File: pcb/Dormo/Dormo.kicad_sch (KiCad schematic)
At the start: 41 parts, among them J1 Conn_01x02_Socket, J2 USB_C_Receptacle_USB2.0_16P, Q1 AO3401A, SW1 SW_DPST, U1 ESP32-C3, U2 MIC5504-3.3YM5, U3 BRCL4054BME, Y1 40MHz

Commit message: cleanup schematic
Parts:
- removed C1: C_Small, symbol Device:C_Small
- removed C3: 100nF, Capacitor_SMD:C_0603_1608Metric_Pad1.08x0.95mm_HandSolder, symbol Device:C_Small
- removed C5: 10uF, Capacitor_SMD:C_0805_2012Metric_Pad1.18x1.45mm_HandSolder, symbol Device:C_Small
- removed J1: Conn_01x02_Socket, symbol Connector:Conn_01x02_Socket
- removed R1: R_Small, symbol Device:R_Small
- added J3: FPC, 6P, P=0.5mm, Connector_FFC-FPC:Hirose_FH12-6S-0.5SH_1x06-1MP_P0.50mm_Horizontal, symbol Connector_Generic:Conn_01x06
- added J4: Conn_01x02, symbol Connector_Generic:Conn_01x02
- SW1: value SW_DPST -> ~
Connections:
- net +3V3: now also J3.6 (Pin_6)
- net +VBAT: now also J3.4 (Pin_4), J4.1 (Pin_1)
- net BTN: now also J3.1 (Pin_1)
- net GND: now also J3.5 (Pin_5), J4.2 (Pin_2)
- net GPIO02: now also J3.2 (Pin_2)
- net GPIO08: now also J3.3 (Pin_3)
- net at C4.1, Y1.3: now also U1.30 (XTAL_P); no longer U1.29 (XTAL_N)
- net at C10.1, Y1.1: now also U1.29 (XTAL_N); no longer U1.30 (XTAL_P)
- net GPIO06: now reaches U1.12 (MTCK)
- net GPIO07: now reaches U1.13 (MTDO)
- net GPIO09: now reaches U1.15 (GPIO9)
- net GPIO10: now reaches U1.16 (GPIO10)
- net GPIO12: now reaches U1.19 (SPIHD)
- net GPIO13: now reaches U1.20 (SPIWP)
- net GPIO14: now reaches U1.21 (SPICS0)
- net GPIO15: now reaches U1.22 (SPICLK)
- net GPIO16: now reaches U1.23 (SPID)
- net GPIO17: now reaches U1.24 (SPIQ)
- net GPIO20: now reaches U1.27 (U0RXD)
- net GPIO21: now reaches U1.28 (U0TXD)
- net GPIO03 renamed EN_VSENSE
- net USB+ renamed GPIO19
- net USB- renamed GPIO18
- net VDD_SPI renamed GPIO11
- no-connect marks 3 -> 2
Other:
- note added: "Battery connector"
- note added: "Check footprint"
- note added: "Pin mapping"
- note added: "Power latch"
- note added: "USB-C connector"
- note added: "VBAT sensing"
- note added: "expander connector"
- note added: "pullups"
- moved on the sheet: AE1, C10, C11, C12, C13, C14, C2, C4, C6, C7, C8, C9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

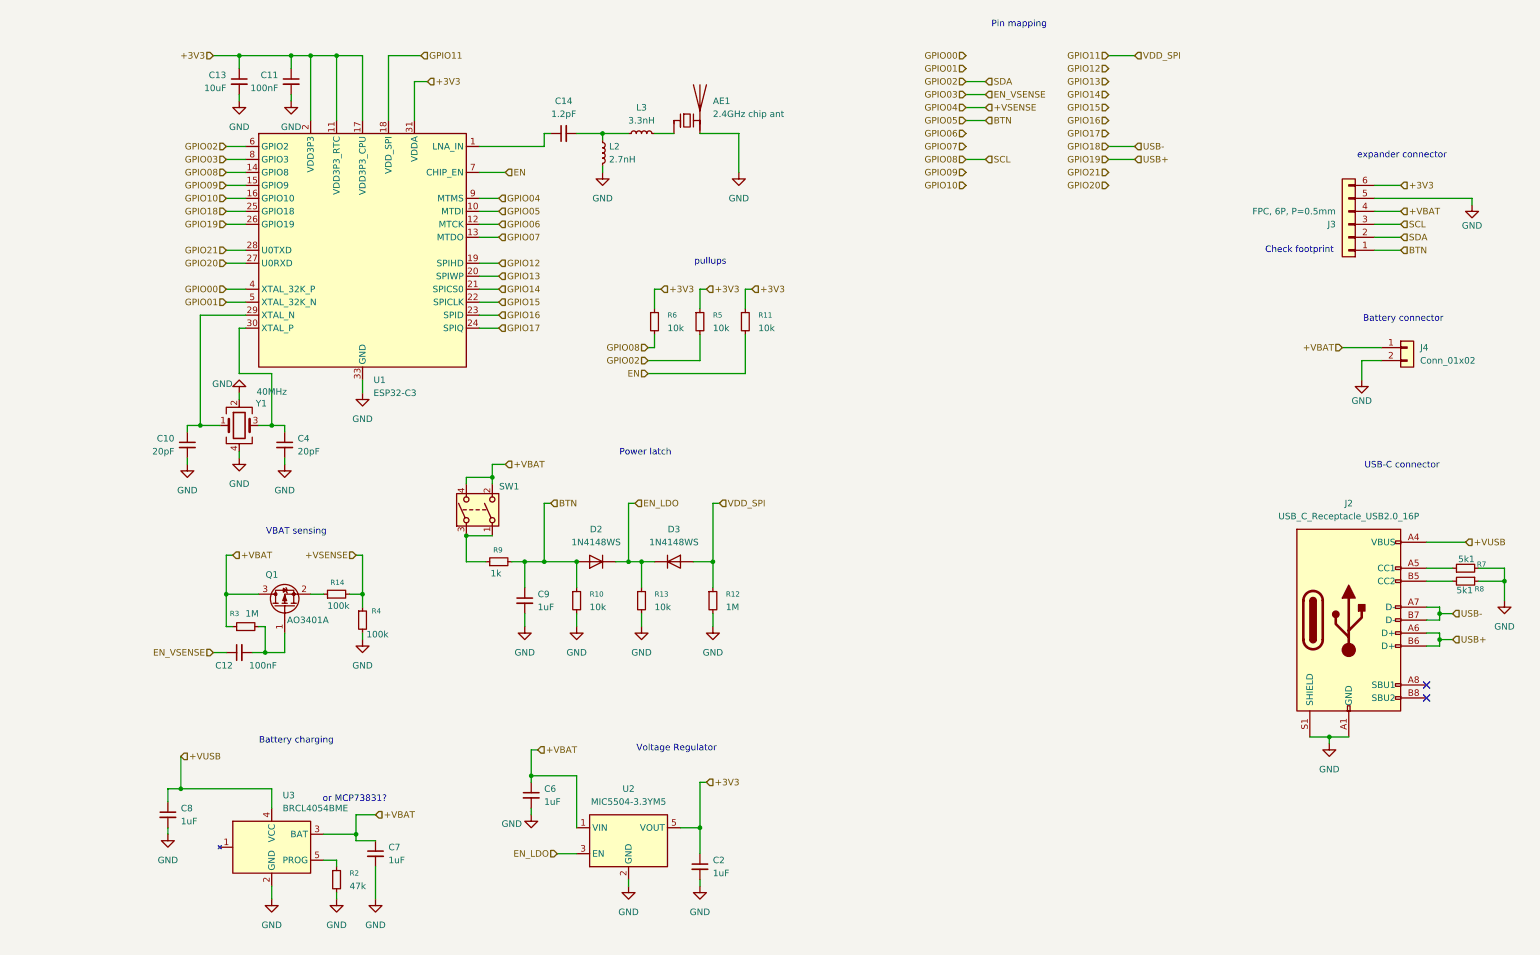
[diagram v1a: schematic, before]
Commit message: added button matrix in schematic
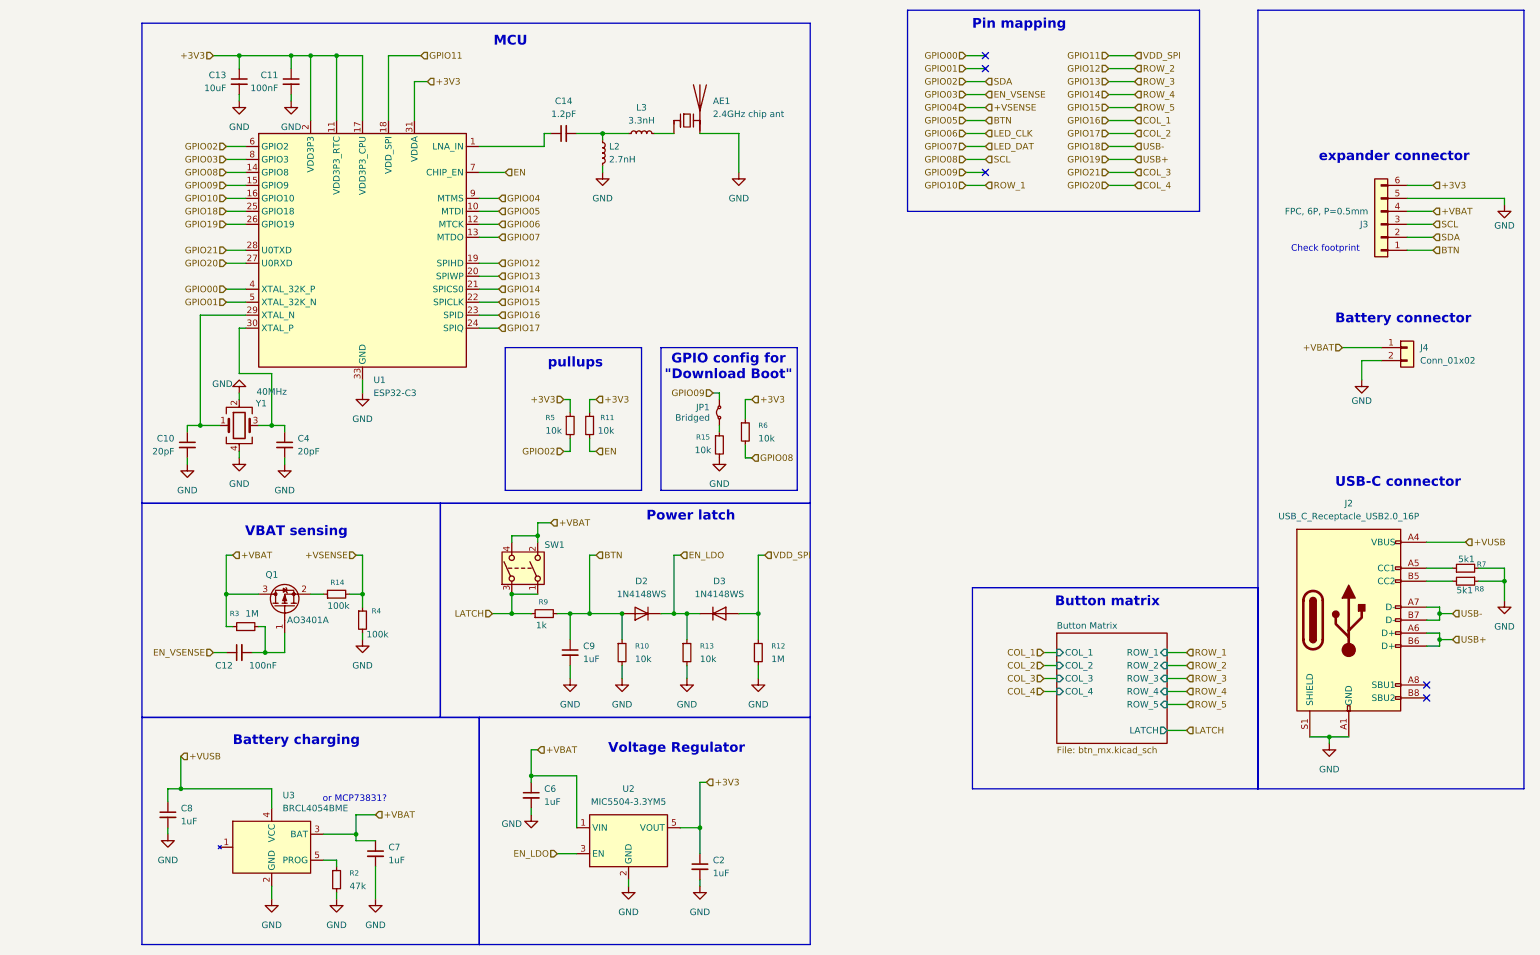
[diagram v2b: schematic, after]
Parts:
- added JP1: Bridged, Jumper:SolderJumper-2_P1.3mm_Bridged_RoundedPad1.0x1.5mm, symbol Jumper:Jumper_2_Small_Bridged
- added R15: 10k, Resistor_SMD:R_0603_1608Metric_Pad0.98x0.95mm_HandSolder, symbol Device:R_Small
- C14: footprint (none) -> Capacitor_SMD:C_0402_1005Metric_Pad0.74x0.62mm_HandSolder; LCSC (none) -> C76899
- J2: footprint (none) -> Connector_USB:USB_C_Receptacle_G-Switch_GT-USB-7010ASV
- J4: footprint (none) -> Connector_PinHeader_2.00mm:PinHeader_1x02_P2.00mm_Horizontal
- L2: footprint (none) -> Inductor_SMD:L_0402_1005Metric_Pad0.77x0.64mm_HandSolder; LCSC (none) -> C77108
- L3: footprint (none) -> Inductor_SMD:L_0402_1005Metric_Pad0.77x0.64mm_HandSolder; LCSC (none) -> C98061
- SW1: footprint (none) -> Button_Switch_SMD:SW_Push_1P1T_XKB_TS-1187A
- U3: LCSC C328563 -> C305436
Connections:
- net GND: now also R15.2
- net GPIO09: now also JP1.2 (B)
- net LATCH: now reaches R9.1, SW1.1, SW1.3
- net GPIO16 renamed COL_1
- net GPIO17 renamed COL_2
- net GPIO20 renamed COL_4
- net GPIO21 renamed COL_3
- new net: JP1.1 (A), R15.1
- no-connect marks 2 -> 5
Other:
- added sheet Button Matrix (btn_mx.kicad_sch)
- note added: "Button matrix"
- note added: "GPIO config for "Download Boot""
- note added: "MCU"
- moved on the sheet: C9, D2, D3, J3, R10, R11, R12, R13, R5, R6, R9, SW1

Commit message: first pcb components layout
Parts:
- J4: footprint Connector_PinHeader_2.00mm:PinHeader_1x02_P2.00mm_Horizontal -> Connector_PinHeader_2.00mm:PinHeader_1x02_P2.00mm_Vertical
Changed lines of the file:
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@@
 			)
 		)
-		(property "Footprint" "Connector_PinHeader_2.00mm:PinHeader_1x02_P2.00mm_Horizontal"
+		(property "Footprint" "Connector_PinHeader_2.00mm:PinHeader_1x02_P2.00mm_Vertical"
 			(at 261.62 78.74 0)
 			(effects

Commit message: first pass of PCB routing
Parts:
- added JP2: Bridged, Jumper:SolderJumper-2_P1.3mm_Bridged_RoundedPad1.0x1.5mm, symbol Jumper:Jumper_2_Small_Bridged
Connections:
- net EN_LDO: now also JP2.1 (A)
- net LATCH: no longer names the net of R9.1, SW1.1, SW1.3
- new net LATCH_MX: JP2.2 (B)
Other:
- note added: "LEDs"
- moved on the sheet: C9, D2, R10, R13, R9, SW1
